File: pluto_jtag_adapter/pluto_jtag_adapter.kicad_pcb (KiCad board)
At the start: 2 copper layers, 53 x 34.2 mm, 61 parts, among them J1 JTAG_UART_PLUTO, J2 Conn_01x08, J3 Conn_01x04, J4 USB_B_Micro, U1 FT2232HL, U2 AP2112K-3.3, U3 AP2112K-1.8, U4 93LC46B, U6 TXB0104D, U7 TLV7031DBV, U8 WE-TVS-82400102, U9 TXB0102DCU, Y1 7M-12.000MAAJ-T

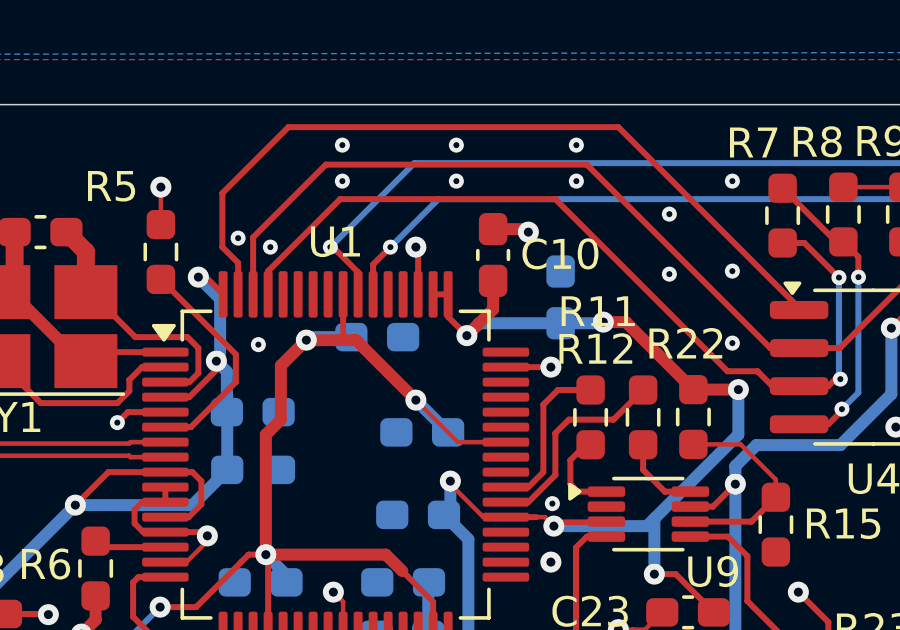
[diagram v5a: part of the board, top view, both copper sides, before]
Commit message: Disconnect VREGIN and VREGOUT
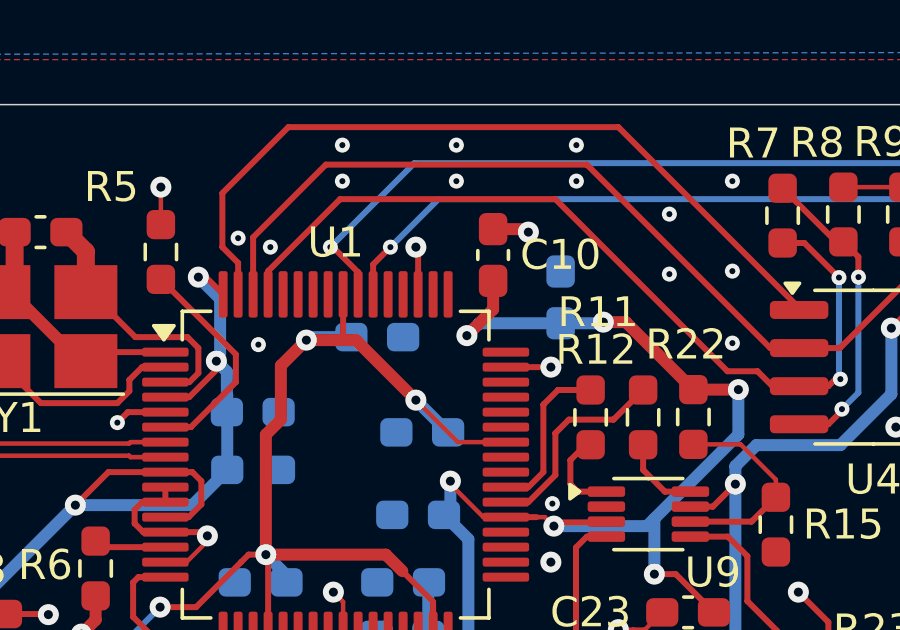
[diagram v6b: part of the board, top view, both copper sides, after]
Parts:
- R6: value 12K -> 1K
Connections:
- U1 pad 49: +1V8 -> unconnected-(U1-VREGOUT-Pad49)
- U1 pad 50: +1V8 -> unconnected-(U1-VREGIN-Pad50)
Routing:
- net +1V8: track 129.6 -> 127.5 mm
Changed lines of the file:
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@@
 	(net 79 "Net-(U9-OE)")
 	(net 80 "Net-(U9-A2)")
+	(net 81 "unconnected-(U1-VREGOUT-Pad49)")
+	(net 82 "unconnected-(U1-VREGIN-Pad50)")
 	(footprint "Resistor_SMD:R_0603_1608Metric_Pad0.98x0.95mm_HandSolder"
 		(layer "F.Cu")
@@
 			(layers "F.Cu" "F.Paste" "F.Mask")
 			(roundrect_rratio 0.25)
-			(net 1 "+1V8")
+			(net 81 "unconnected-(U1-VREGOUT-Pad49)")
 			(pinfunction "VREGOUT")
 			(pintype "power_out")
@@
 			(layers "F.Cu" "F.Paste" "F.Mask")
 			(roundrect_rratio 0.25)
-			(net 1 "+1V8")
+			(net 82 "unconnected-(U1-VREGIN-Pad50)")
 			(pinfunction "VREGIN")
 			(pintype "power_in")
@@
 			)
 		)
-		(property "Value" "12K"
+		(property "Value" "1K"
 			(at -2.25 0.25 0)
 			(layer "F.Fab")
@@
 	)
 	(segment
-		(start 124.325 86.325)
-		(end 124.325 85.575)
-		(width 0.2)
-		(layer "F.Cu")
-		(net 1)
-	)
-	(segment
 		(start 105.72 97.885)
 		(end 105.775 97.94)
@@
 	)
 	(segment
-		(start 123.825 85.575)
-		(end 124.325 85.575)
-		(width 0.2)
-		(layer "F.Cu")
-		(net 1)
-	)
-	(segment
 		(start 115.674999 93)
 		(end 116.1 92.574999)
@@
 		(width 0.2)
 		(layer "F.Cu")
-		(net 1)
-	)
-	(segment
-		(start 124.95 86.95)
-		(end 124.325 86.325)
-		(width 0.2)
-		(layer "F.Cu")
